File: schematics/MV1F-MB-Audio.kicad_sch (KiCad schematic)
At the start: 54 parts, among them J1 HEADPHONES, U1 6116, U4 NEO-DO, U7 YM3016D, U8 NJM2066D, X3 24MHz

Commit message: complete DaughterBoard
rename sub files
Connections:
- net SDMRO is gone; now on net SDMRD: 3K.22 (CS), U1.20 (OE)
- net SDRD0: no longer 2L.17 (RAD0)
- net SDRD1: no longer 2L.16 (RAD1)
- net SDPOB renamed SDPOE
- net SDRD2 renamed SDRAD2
- net SDRD3 renamed SDRAD3
- net SDRD4 renamed SDRAD4
- net SDRD5 renamed SDRAD5
- net SDRD6 renamed SDRAD6
- net SDRD7 renamed SDRAD7
- net SDROB renamed SDROE
- net SDROH renamed SDROM
- new net SDRAD0: 2L.17 (RAD0)
- new net SDRAD1: 2L.16 (RAD1)

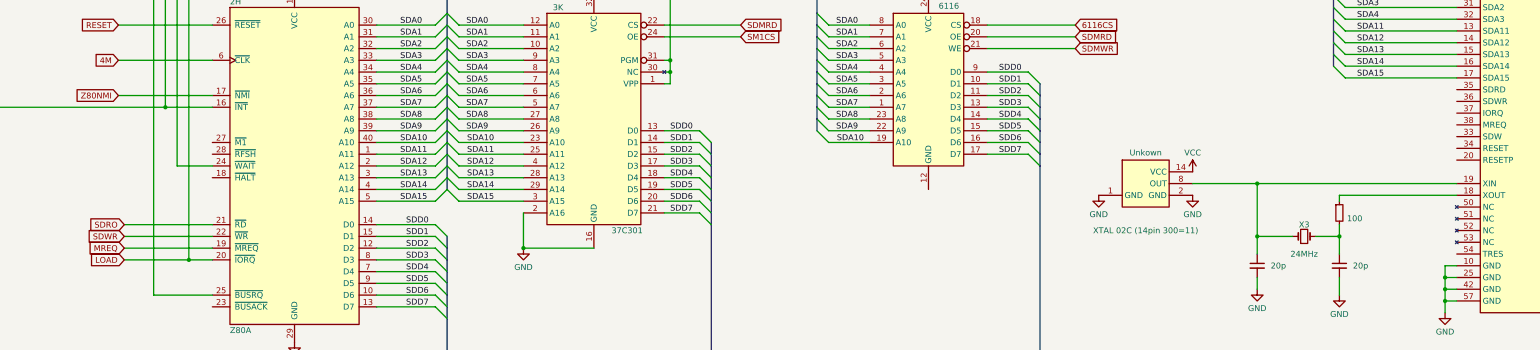
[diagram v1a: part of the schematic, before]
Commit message: Typo... and orphan labels remove
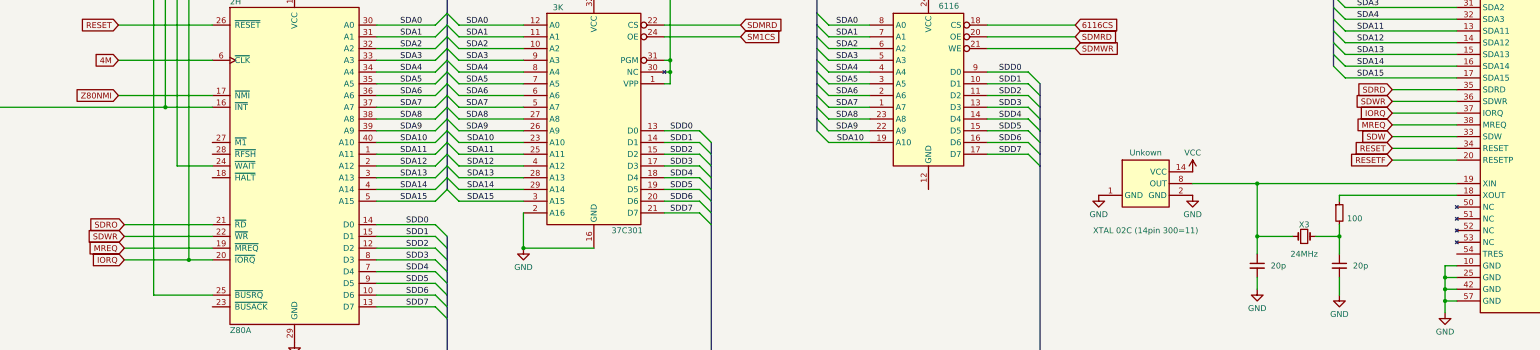
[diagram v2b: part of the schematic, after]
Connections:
- net LOAD is gone; now on net IORQ: 2H.20 (~{IORQ}), RN2.5 (R4)
- net MREQ: now also U4.38 (MREQ)
- net RESET: now also U4.34 (RESET)
- net SDWR: now also U4.36 (SDWR)
- net RESETF: now reaches U4.20 (RESETP)
- net SDW: now reaches U4.33 (SDW)
- net SDRD: now reaches U4.35 (SDRD)
- net IORQ: now reaches U4.37 (IORQ)
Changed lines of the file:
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@@
+    (stroke (width 0) (type default))
+  )
+  (wire (pts (xy 345.44 85.09) (xy 359.41 85.09))
     (stroke (width 0) (type default))
   )
@@
     (stroke (width 0) (type default))
   )
+  (wire (pts (xy 345.44 72.39) (xy 359.41 72.39))
+    (stroke (width 0) (type default))
+  )
   (wire (pts (xy 394.97 54.61) (xy 425.45 54.61))
     (stroke (width 0) (type default))
@@
     (stroke (width 0) (type default))
   )
+  (wire (pts (xy 345.44 87.63) (xy 359.41 87.63))
+    (stroke (width 0) (type default))
+  )
   (wire (pts (xy 328.93 104.14) (xy 334.01 104.14))
     (stroke (width 0) (type default))
@@
     (stroke (width 0) (type default))
   )
+  (wire (pts (xy 345.44 77.47) (xy 359.41 77.47))
+    (stroke (width 0) (type default))
+  )
   (bus (pts (xy 116.84 182.88) (xy 116.84 185.42))
     (stroke (width 0) (type default))
@@
     (stroke (width 0) (type default))
   )
+  (wire (pts (xy 345.44 82.55) (xy 359.41 82.55))
+    (stroke (width 0) (type default))
+  )
   (wire (pts (xy 125.73 73.66) (xy 138.43 73.66))
     (stroke (width 0) (type default))
@@
     (stroke (width 0) (type default))
   )
+  (wire (pts (xy 345.44 74.93) (xy 359.41 74.93))
+    (stroke (width 0) (type default))
+  )
   (wire (pts (xy 43.18 187.96) (xy 62.23 187.96))
     (stroke (width 0) (type default))
@@
   )
   (wire (pts (xy 200.66 311.15) (xy 222.25 311.15))
+    (stroke (width 0) (type default))
+  )
+  (wire (pts (xy 345.44 80.01) (xy 359.41 80.01))
     (stroke (width 0) (type default))
   )
@@
     )
   )
+  (global_label "IORQ" (shape input) (at 345.44 77.47 180) (fields_autoplaced)
+    (effects (font (size 1.27 1.27)) (justify right))
+    (property "Intersheetrefs" "${INTERSHEET_REFS}" (at 337.919 77.47 0)
+      (effects (font (size 1.27 1.27)) (justify right))
+    )
+  )
   (global_label "SDRA22" (shape input) (at 99.06 162.56 0) (fields_autoplaced)
     (effects (font (size 1.27 1.27)) (justify left))
@@
     )
   )
+  (global_label "RESET" (shape input) (at 345.44 85.09 180) (fields_autoplaced)
+    (effects (font (size 1.27 1.27)) (justify right))
+    (property "Intersheetrefs" "${INTERSHEET_REFS}" (at 336.7097 85.09 0)
+      (effects (font (size 1.27 1.27)) (justify right))
+    )
+  )
+  (global_label "SDRD" (shape input) (at 345.44 72.39 180) (fields_autoplaced)
+    (effects (font (size 1.27 1.27)) (justify right))
+    (property "Intersheetrefs" "${INTERSHEET_REFS}" (at 337.4353 72.39 0)
+      (effects (font (size 1.27 1.27)) (justify right))
+    )
+  )
   (global_label "2610CS" (shape input) (at 43.18 193.04 180) (fields_autoplaced)
     (effects (font (size 1.27 1.27)) (justify right))
@@
     )
   )
+  (global_label "SDWR" (shape input) (at 345.44 74.93 180) (fields_autoplaced)
+    (effects (font (size 1.27 1.27)) (justify right))
+    (property "Intersheetrefs" "${INTERSHEET_REFS}" (at 337.2539 74.93 0)
+      (effects (font (size 1.27 1.27)) (justify right))
+    )
+  )
   (global_label "Z80NMI" (shape input) (at 69.85 73.66 180) (fields_autoplaced)
     (effects (font (size 1.27 1.27)) (justify right))
@@
     )
   )
+  (global_label "SDW" (shape input) (at 345.44 82.55 180) (fields_autoplaced)
+    (effects (font (size 1.27 1.27)) (justify right))
+    (property "Intersheetrefs" "${INTERSHEET_REFS}" (at 338.5239 82.55 0)
+      (effects (font (size 1.27 1.27)) (justify right))
+    )
+  )
   (global_label "6116CS" (shape input) (at 425.45 57.15 0) (fields_autoplaced)
     (effects (font (size 1.27 1.27)) (justify left))
@@
     )
   )
+  (global_label "RESETF" (shape input) (at 345.44 87.63 180) (fields_autoplaced)
+    (effects (font (size 1.27 1.27)) (justify right))
+    (property "Intersheetrefs" "${INTERSHEET_REFS}" (at 335.6211 87.63 0)
+      (effects (font (size 1.27 1.27)) (justify right))
+    )
+  )
   (global_label "SDWR" (shape input) (at 71.12 104.14 180) (fields_autoplaced)
     (effects (font (size 1.27 1.27)) (justify right))
@@
     )
   )
-  (global_label "LOAD" (shape input) (at 71.12 109.22 180) (fields_autoplaced)
-    (effects (font (size 1.27 1.27)) (justify right))
-    (property "Intersheetrefs" "${INTERSHEET_REFS}" (at 63.4176 109.22 0)
+  (global_label "IORQ" (shape input) (at 71.12 109.22 180) (fields_autoplaced)
+    (effects (font (size 1.27 1.27)) (justify right))
+    (property "Intersheetrefs" "${INTERSHEET_REFS}" (at 63.599 109.22 0)
       (effects (font (size 1.27 1.27)) (justify right))
     )
@@
     )
   )
+  (global_label "MREQ" (shape input) (at 345.44 80.01 180) (fields_autoplaced)
+    (effects (font (size 1.27 1.27)) (justify right))
+    (property "Intersheetrefs" "${INTERSHEET_REFS}" (at 337.2539 80.01 0)
+      (effects (font (size 1.27 1.27)) (justify right))
+    )
+  )
